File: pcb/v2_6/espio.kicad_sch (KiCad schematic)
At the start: 27 parts, among them J1 Conn_Dbg_Header, J2 Conn_01x08, J3 Conn_01x09, J4 Conn_01x01, J5 Conn_01x08, J6 Conn_01x08, Q1 2SC1623 300-400, U1 MCP2562-E-SN, U5 LF50CPT-TR, U6 14.4

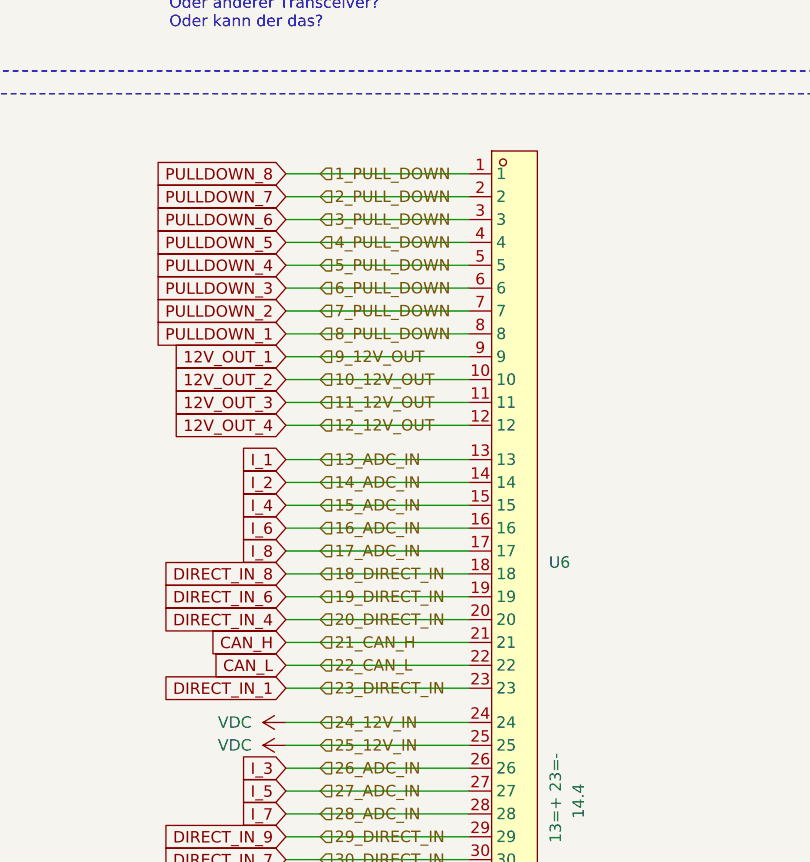
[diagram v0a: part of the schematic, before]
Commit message: Refactor, fix external LED conflict
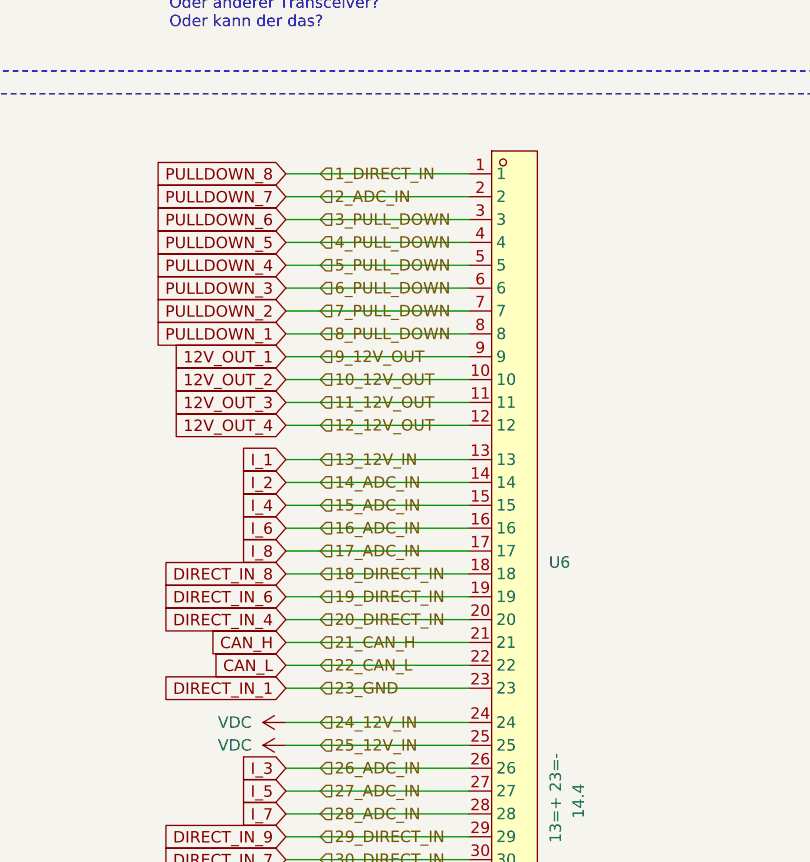
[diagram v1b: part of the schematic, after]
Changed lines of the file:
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@@
 		)
 	)
-	(hierarchical_label "23_DIRECT_IN"
+	(hierarchical_label "23_GND"
 		(shape input)
 		(at 347.98 146.05 0)
@@
 		)
 	)
-	(hierarchical_label "13_ADC_IN"
+	(hierarchical_label "13_12V_IN"
 		(shape input)
 		(at 347.98 120.65 0)
@@
 		)
 	)
-	(hierarchical_label "1_PULL_DOWN"
+	(hierarchical_label "1_DIRECT_IN"
 		(shape input)
 		(at 347.98 88.9 0)
@@
 		)
 	)
-	(hierarchical_label "2_PULL_DOWN"
+	(hierarchical_label "2_ADC_IN"
 		(shape input)
 		(at 347.98 91.44 0)
